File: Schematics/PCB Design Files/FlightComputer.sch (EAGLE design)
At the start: 9 parts

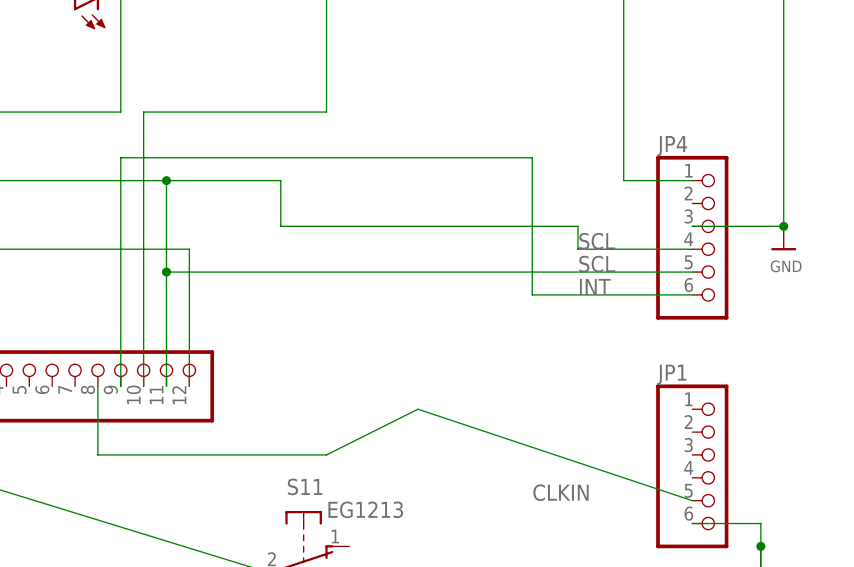
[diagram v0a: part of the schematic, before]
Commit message: Created header files for simplicity and abstracted code for cleanliness
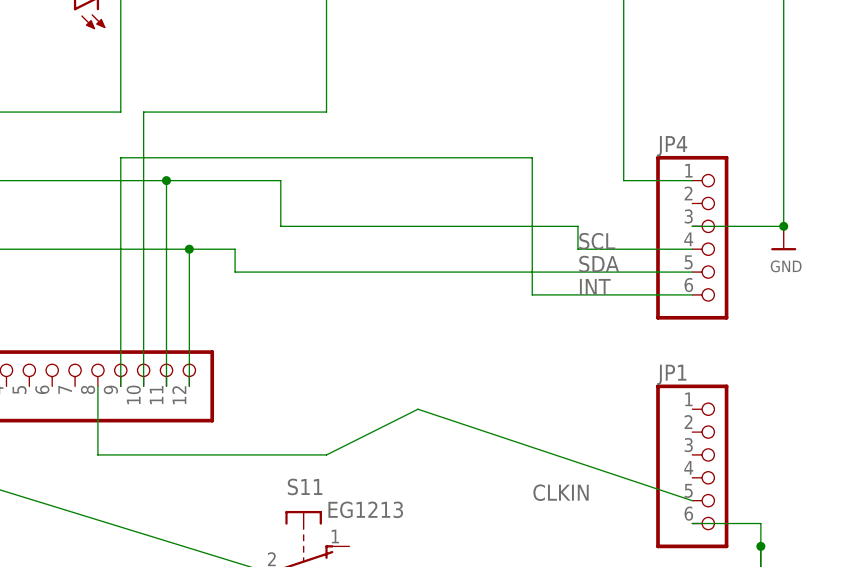
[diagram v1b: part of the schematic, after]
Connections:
- net SCL: no longer JP4.5
- net SDA: now also JP4.5
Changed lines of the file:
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@@
 <junction x="83.82" y="81.28"/>
 <pinref part="JP3" gate="G$1" pin="11"/>
-<wire x1="83.82" y1="81.28" x2="83.82" y2="71.12" width="0.1524" layer="91"/>
-<pinref part="JP4" gate="A" pin="5"/>
-<wire x1="83.82" y1="71.12" x2="83.82" y2="58.42" width="0.1524" layer="91"/>
-<wire x1="142.24" y1="71.12" x2="83.82" y2="71.12" width="0.1524" layer="91"/>
-<label x="129.54" y="71.12" size="1.778" layer="95"/>
-<junction x="83.82" y="71.12"/>
+<wire x1="83.82" y1="81.28" x2="83.82" y2="58.42" width="0.1524" layer="91"/>
 </segment>
 </net>
@@
 <pinref part="JP3" gate="G$1" pin="12"/>
 <wire x1="86.36" y1="58.42" x2="86.36" y2="73.66" width="0.1524" layer="91"/>
+<pinref part="JP4" gate="A" pin="5"/>
+<wire x1="142.24" y1="71.12" x2="91.44" y2="71.12" width="0.1524" layer="91"/>
+<wire x1="91.44" y1="71.12" x2="91.44" y2="73.66" width="0.1524" layer="91"/>
+<wire x1="91.44" y1="73.66" x2="86.36" y2="73.66" width="0.1524" layer="91"/>
+<junction x="86.36" y="73.66"/>
+<label x="129.54" y="71.12" size="1.778" layer="95"/>
 </segment>
 </net>
